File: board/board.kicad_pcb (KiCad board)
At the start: 2 copper layers, 45 x 45 mm, 10 parts, among them J1 010_UART, J2 002_SPI, J3 011_GPIO, J4 001_I2C, U1 ESP32-S3-WROOM-1

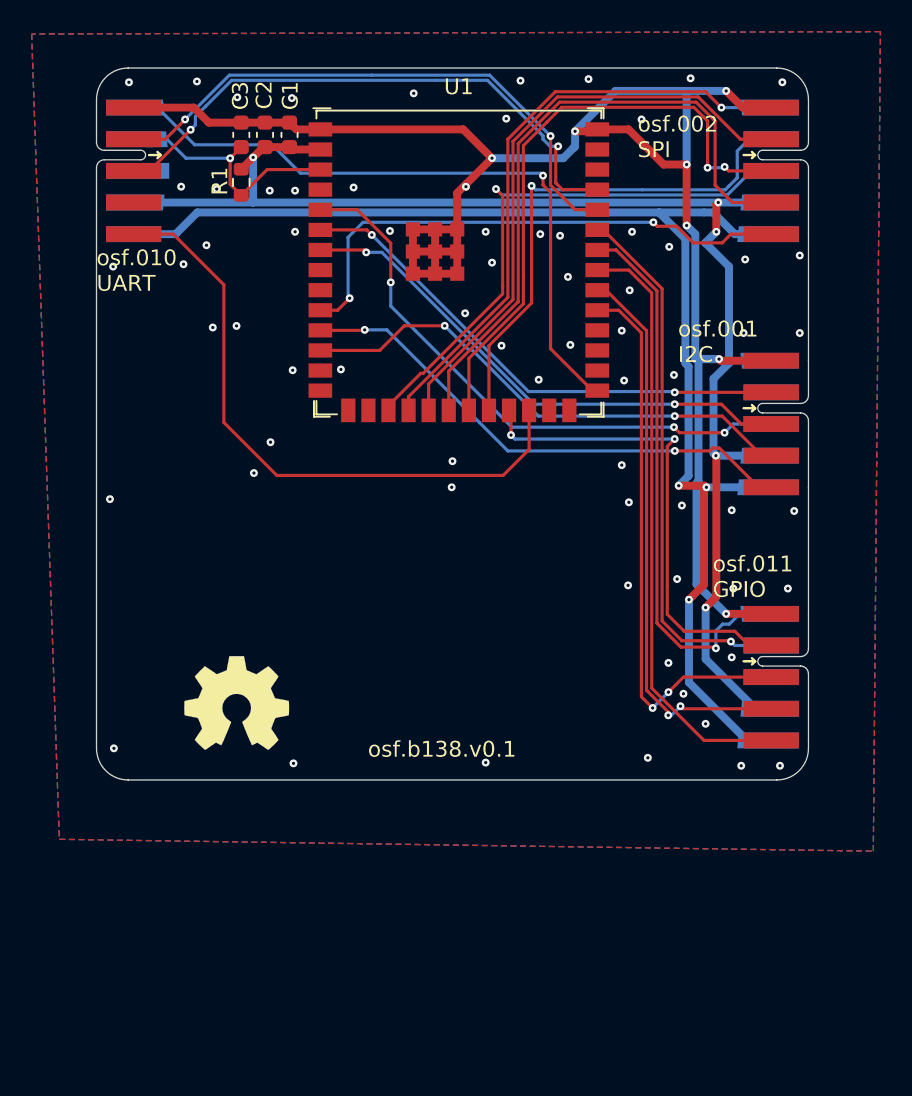
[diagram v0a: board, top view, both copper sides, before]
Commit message: added usb and ADC connectors
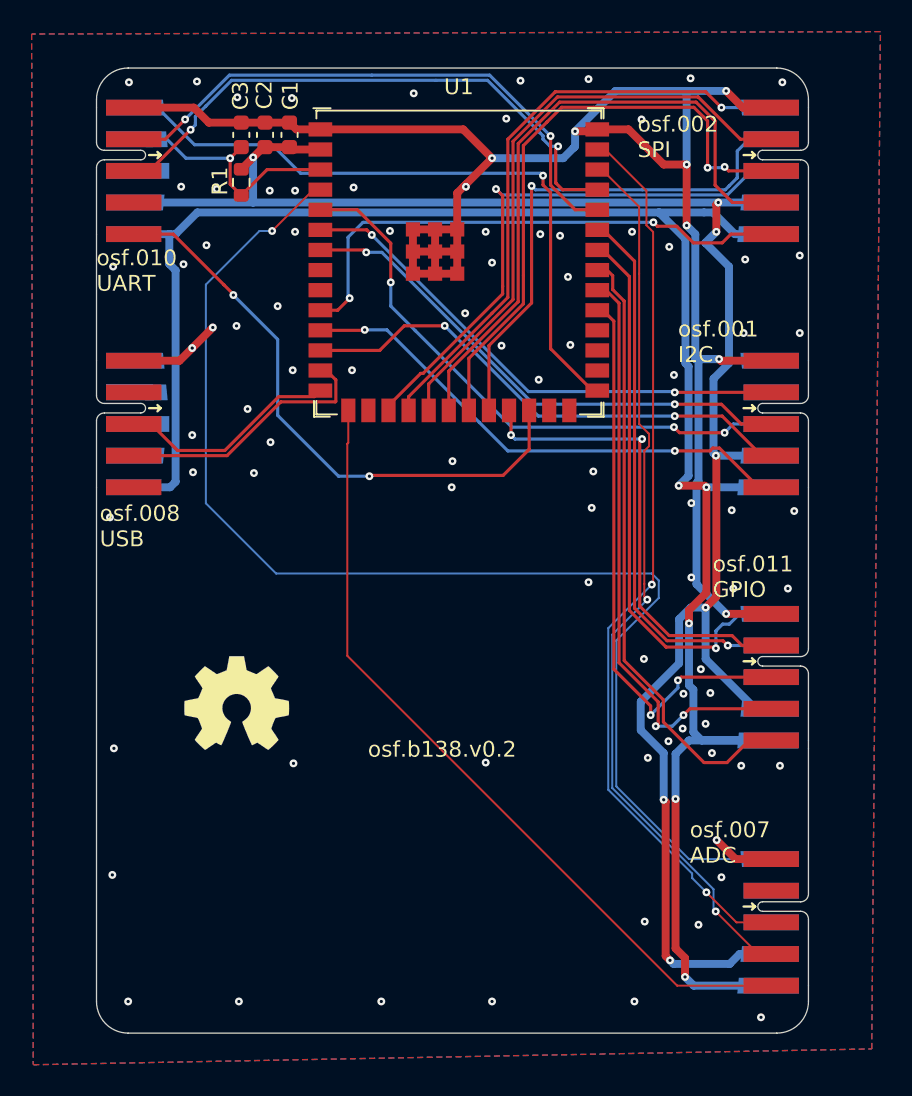
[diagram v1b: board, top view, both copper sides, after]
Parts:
- added J5: 007_ADC, on_edge:on_edge_2x05_host, F.Cu at (185.0, 144.0)
- added J6: 008_USB, on_edge:on_edge_2x05_device, F.Cu at (140.0, 112.5)
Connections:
- U1 pad 15: unconnected-(U1-GPIO3/TOUCH3/ADC1_CH2-Pad15) -> /esp/ADC2
- U1 pad 38: unconnected-(U1-GPIO2/TOUCH2/ADC1_CH1-Pad38) -> /esp/ADC1
- U1 pad 39: unconnected-(U1-GPIO1/TOUCH1/ADC1_CH0-Pad39) -> /esp/ADC0
- U1 pad 4: unconnected-(U1-GPIO4/TOUCH4/ADC1_CH3-Pad4) -> /esp/ADC3
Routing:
- net /esp/ADC3: track 0.00 -> 80.0 mm, vias 0 -> 1
- net /esp/ADC0: track 0.00 -> 57.3 mm, vias 0 -> 2
- net /esp/ADC1: track 0.00 -> 56.9 mm, vias 0 -> 2
- net /esp/ADC2: track 0.00 -> 51.0 mm
- net +5V: track 84.7 -> 131.2 mm, vias 3 -> 5
- net +3.3V: track 88.1 -> 120.1 mm, vias 5 -> 7
- net /esp/USB_D-: track 0.00 -> 16.8 mm
- net /esp/USB_D+: track 0.00 -> 14.1 mm
- net GND: track 117.8 -> 127.6 mm, vias 76 -> 93
- net /esp/U0_INT: track 39.6 -> 37.3 mm, vias 0 -> 2
- net /esp/IO2: track 35.9 -> 37.3 mm
- net /esp/IO3: track 37.9 -> 39.1 mm
- net /esp/IO0: track 30.7 -> 30.0 mm
- net /esp/IO5: track 34.2 -> 34.7 mm
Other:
- board size 45 x 45 mm -> 45 x 61 mm
- board text added: "osf.007 ADC"
- board text added: "osf.008 USB"
- board text added: "osf.b138.v0.2"
- board text removed: "osf.b138.v0.1"
